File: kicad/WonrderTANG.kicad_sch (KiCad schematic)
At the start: 30 parts, among them CON1 MSX-CONNECTOR, J2 AudioJack3, J3 Conn_02x03_Odd_Even, U1 SN74LVC245AN, U2 SN74LVC245AN, U3 SN74LVC245AN, U48 MCP6281, U5 SN74LVC245AN, U6 Tang_Nano_20k, U7 SN74LVC245AN

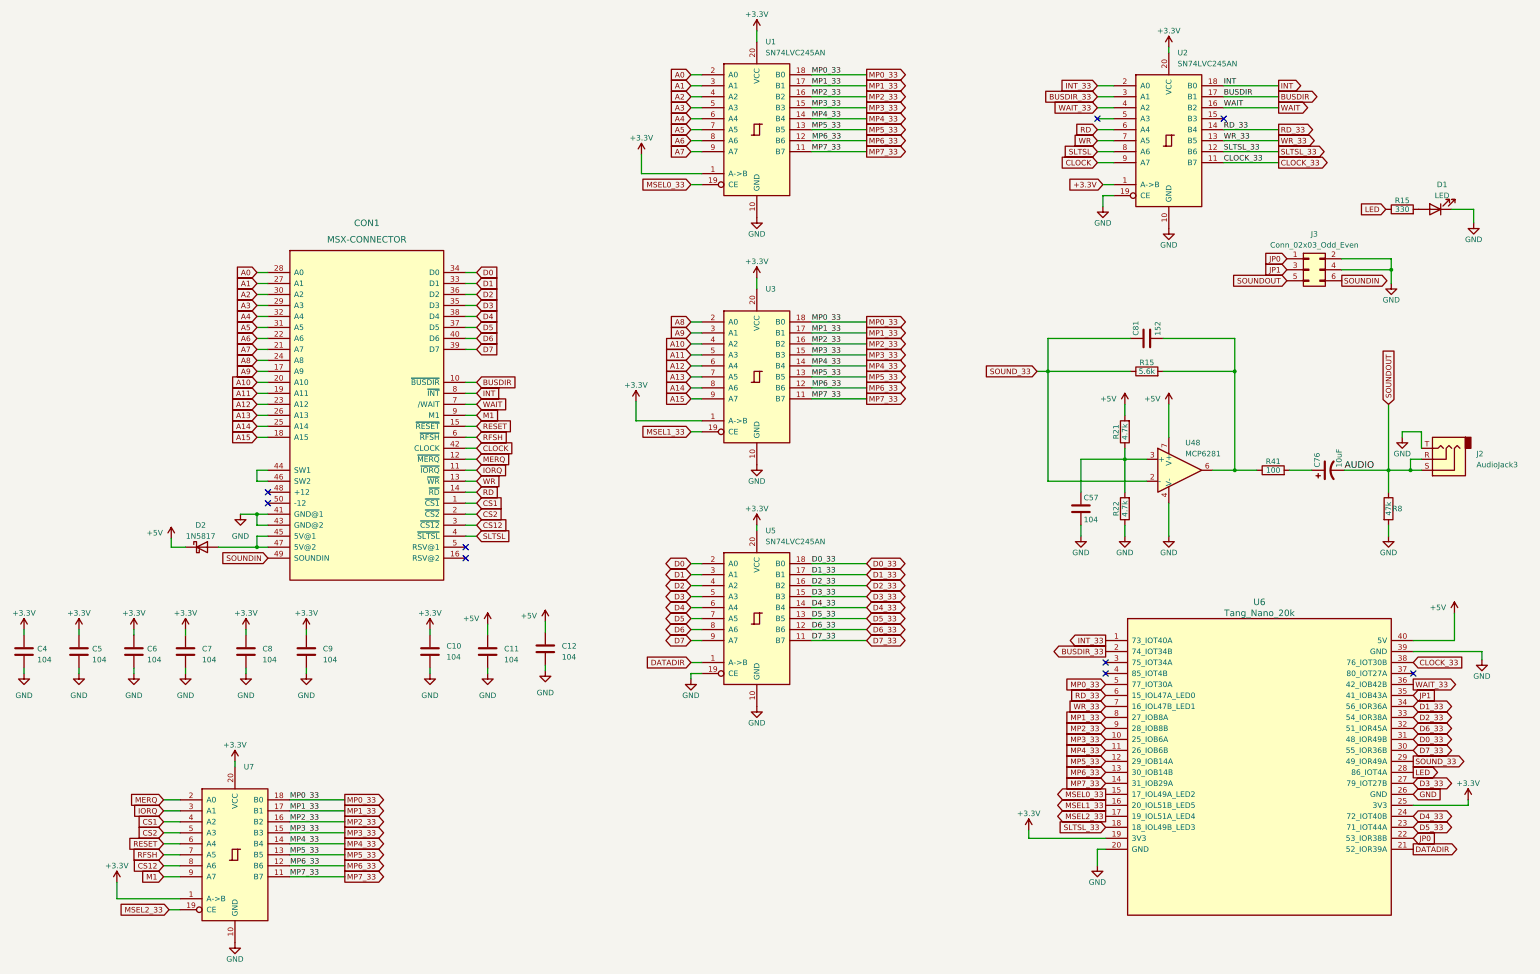
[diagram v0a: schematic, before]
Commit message: fix on wait line
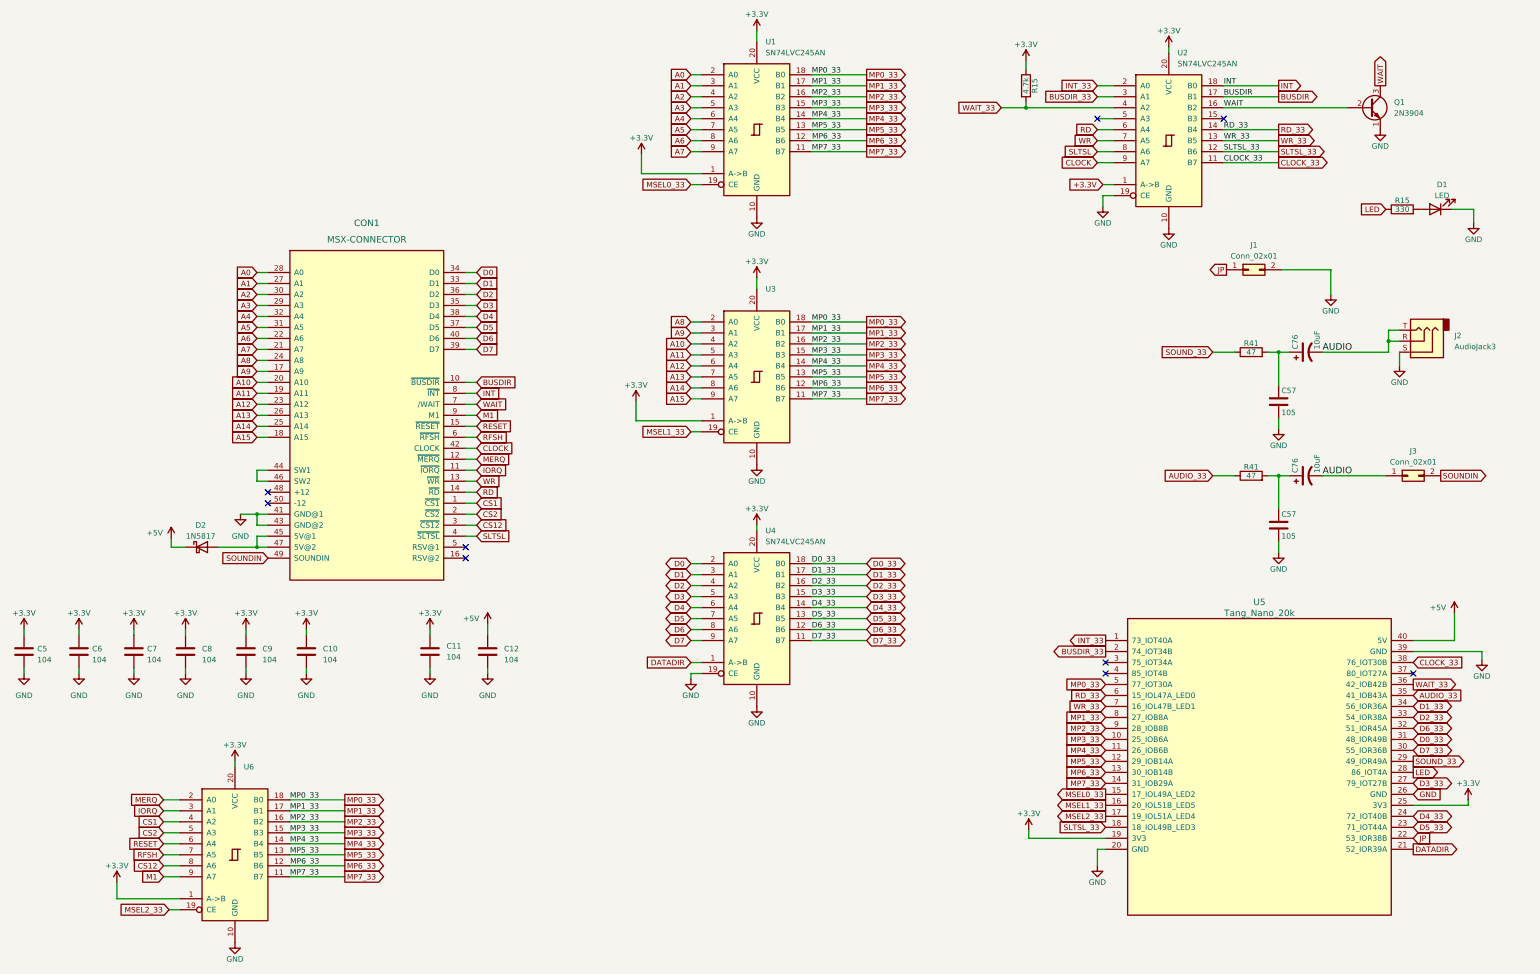
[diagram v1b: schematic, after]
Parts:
- removed C12: 104, Capacitor_THT:C_Disc_D5.0mm_W2.5mm_P2.50mm, symbol Device:C
- removed C81: 152, Capacitor_THT:C_Disc_D5.0mm_W2.5mm_P2.50mm, symbol Device:C
- removed J3: Conn_02x03_Odd_Even, Connector_PinHeader_2.54mm:PinHeader_2x03_P2.54mm_Vertical, symbol Connector_Generic:Conn_02x03_Odd_Even
- removed R21, R22: 4.7k, Resistor_THT:R_Axial_DIN0204_L3.6mm_D1.6mm_P5.08mm_Horizontal, symbol Device:R
- removed R8: 47k, Resistor_THT:R_Axial_DIN0204_L3.6mm_D1.6mm_P5.08mm_Horizontal, symbol Device:R
- removed U48: MCP6281, Package_DIP:DIP-8_W7.62mm_Socket_LongPads, symbol Amplifier_Operational:MCP601-xP
- added C57: 105, Capacitor_THT:C_Disc_D5.0mm_W2.5mm_P2.50mm, symbol Device:C
- added C76: 10uF, Capacitor_THT:CP_Radial_D5.0mm_P2.00mm, symbol Omega-Mainboard-rescue:CP1-Device
- added J1, J3: Conn_02x01, Connector_PinHeader_2.54mm:PinHeader_2x01_P2.54mm_Vertical, symbol Connector_Generic:Conn_02x01
- added Q1: 2N3904, Package_TO_SOT_THT:TO-92_Inline, symbol Transistor_BJT:2N3904
- added R41: 47, Resistor_THT:R_Axial_DIN0207_L6.3mm_D2.5mm_P10.16mm_Horizontal, symbol Device:R
- C57: value 104 -> 105
- R15: footprint Resistor_THT:R_Axial_DIN0204_L3.6mm_D1.6mm_P5.08mm_Horizontal -> Resistor_THT:R_Axial_DIN0207_L6.3mm_D2.5mm_P10.16mm_Horizontal
- R15: value 5.6k -> 4.7k; footprint Resistor_THT:R_Axial_DIN0204_L3.6mm_D1.6mm_P5.08mm_Horizontal -> Resistor_THT:R_Axial_DIN0207_L6.3mm_D2.5mm_P10.16mm_Horizontal
- R41: value 100 -> 47; footprint Resistor_THT:R_Axial_DIN0204_L3.6mm_D1.6mm_P5.08mm_Horizontal -> Resistor_THT:R_Axial_DIN0207_L6.3mm_D2.5mm_P10.16mm_Horizontal
- renumbered C9 to C10, C10 to C11, C11 to C12, C4 to C5, C5 to C6, C6 to C7, C7 to C8, C8 to C9, U5 to U4, U6 to U5, U7 to U6
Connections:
- net +3.3V: now also R15.1
- net GND: now also J2.S, C57.2, J1.2 (Pin_2), Q1.1 (E); no longer J2.T
- net SOUNDIN: now also J3.2 (Pin_2)
- net SOUND_33: now also R41.1; no longer R15.1
- net WAIT: now also Q1.2 (B), Q1.3 (C)
- net WAIT_33: now also R15.2
- net at C57.1: now also C76.1, R41.2
- net JP0 renamed JP
- net JP: now also J1.1 (Pin_1)
- net JP1 renamed AUDIO_33
- net AUDIO_33: now also R41.1
- net SOUNDOUT renamed AUDIO
- net AUDIO: now also J2.T, C76.2, J3.1 (Pin_1); no longer J2.S
- new net: C57.1, C76.1, R41.2
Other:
- moved on the sheet: C57, C76, J2, R41

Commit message: kicad fixes
fix shorted transistor add 10uf power line, moved cap to allow be placed horizontally
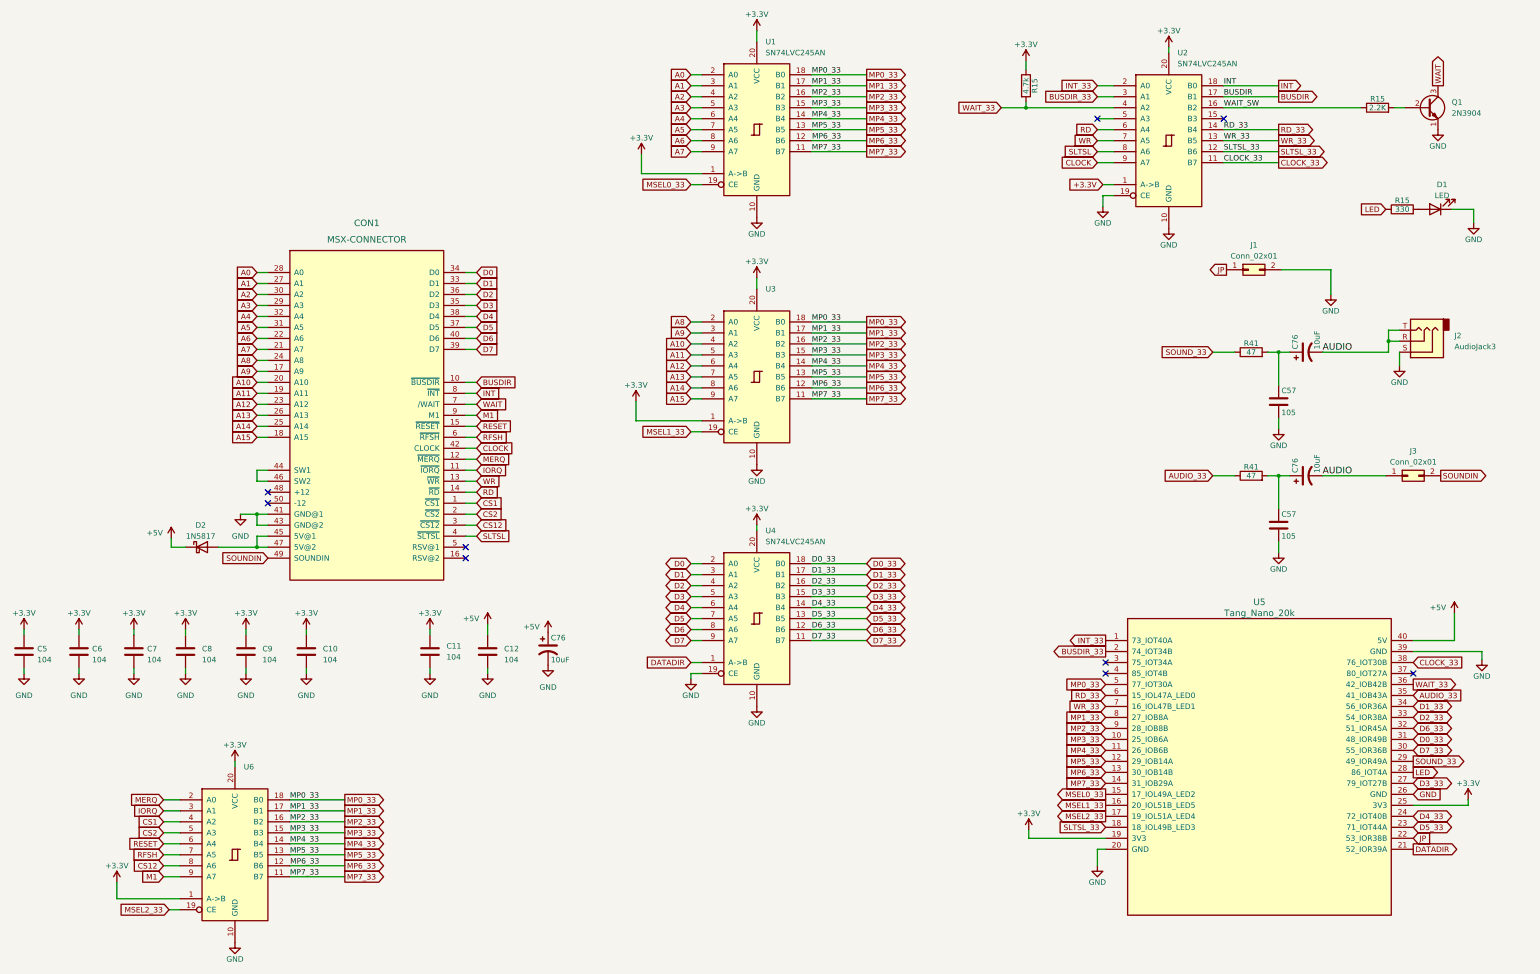
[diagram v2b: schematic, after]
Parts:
- added C76: 10uF, Capacitor_THT:CP_Radial_D5.0mm_P2.00mm, symbol Omega-Mainboard-rescue:CP1-Device
- added R15: 2.2K, Resistor_THT:R_Axial_DIN0207_L6.3mm_D2.5mm_P10.16mm_Horizontal, symbol Device:R
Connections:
- net +5V: now also C76.1
- net GND: now also C76.2
- net WAIT: no longer Q1.2 (B), U2.16 (B2)
- new net: Q1.2 (B), R15.2
- new net WAIT_SW: R15.1, U2.16 (B2)
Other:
- moved on the sheet: Q1
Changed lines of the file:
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@@
     (stroke (width 0) (type default))
   )
-  (wire (pts (xy 325.12 53.34) (xy 353.695 53.34))
-    (stroke (width 0) (type default))
-  )
   (wire (pts (xy 363.22 109.855) (xy 363.22 107.315))
     (stroke (width 0) (type default))
@@
     (stroke (width 0) (type default))
   )
+  (wire (pts (xy 364.49 53.34) (xy 367.03 53.34))
+    (stroke (width 0) (type default))
+  )
   (wire (pts (xy 378.46 176.53) (xy 378.46 170.18))
     (stroke (width 0) (type default))
@@
     (stroke (width 0) (type default))
   )
+  (wire (pts (xy 325.12 53.34) (xy 356.87 53.34))
+    (stroke (width 0) (type default))
+  )
   (wire (pts (xy 97.79 147.32) (xy 101.6 147.32))
     (stroke (width 0) (type default))
@@
     (effects (font (size 1.27 1.27)) (justify left bottom))
   )
-  (label "WAIT" (at 325.12 53.34 0) (fields_autoplaced)
+  (label "WAIT_SW" (at 325.12 53.34 0) (fields_autoplaced)
     (effects (font (size 1.27 1.27)) (justify left bottom))
   )
@@
     )
   )
-  (global_label "WAIT" (shape output) (at 361.315 48.26 90) (fields_autoplaced)
+  (global_label "WAIT" (shape output) (at 374.65 48.26 90) (fields_autoplaced)
     (effects (font (size 1.27 1.27)) (justify left))
-    (property "Intersheetrefs" "${INTERSHEET_REFS}" (at 361.315 41.8166 90)
+    (property "Intersheetrefs" "${INTERSHEET_REFS}" (at 374.65 41.8166 90)
       (effects (font (size 1.27 1.27)) (justify left) hide)
     )
@@
     )
   )
-  (symbol (lib_id "power:GND") (at 361.315 58.42 0) (unit 1)
+  (symbol (lib_id "power:GND") (at 374.65 58.42 0) (unit 1)
     (in_bom yes) (on_board yes) (dnp no)
-    (property "Reference" "#PWR091" (at 361.315 64.77 0)
+    (property "Reference" "#PWR091" (at 374.65 64.77 0)
       (effects (font (size 1.27 1.27)) hide)
     )
-    (property "Value" "GND" (at 361.315 62.23 0)
+    (property "Value" "GND" (at 374.65 62.23 0)
       (effects (font (size 1.27 1.27)))
     )
-    (property "Footprint" "" (at 361.315 58.42 0)
+    (property "Footprint" "" (at 374.65 58.42 0)
       (effects (font (size 1.27 1.27)) hide)
     )
-    (property "Datasheet" "" (at 361.315 58.42 0)
+    (property "Datasheet" "" (at 374.65 58.42 0)
       (effects (font (size 1.27 1.27)) hide)
     )
@@
     )
   )
+  (symbol (lib_id "power:GND") (at 168.91 182.245 0) (unit 1)
+    (in_bom yes) (on_board yes) (dnp no) (fields_autoplaced)
+    (property "Reference" "#PWR047" (at 168.91 188.595 0)
+      (effects (font (size 1.27 1.27)) hide)
+    )
+    (property "Value" "GND" (at 168.91 187.325 0)
+      (effects (font (size 1.27 1.27)))
+    )
+    (property "Footprint" "" (at 168.91 182.245 0)
+      (effects (font (size 1.27 1.27)) hide)
+    )
+    (property "Datasheet" "" (at 168.91 182.245 0)
+      (effects (font (size 1.27 1.27)) hide)
+    )
+    (pin "1")
+    (instances
+      (project "WonrderTANG"
+        (path "/aac9604b-8c84-42de-bd09-e07036aaaac8"
+          (reference "#PWR047") (unit 1)
+        )
+      )
+    )
+  )
   (symbol (lib_id "Device:LED") (at 374.015 76.835 180) (unit 1)
     (in_bom yes) (on_board yes) (dnp no) (fields_autoplaced)
@@
     )
   )
+  (symbol (lib_id "Omega-Mainboard-rescue:CP1-Device") (at 168.91 178.435 0) (unit 1)
+    (in_bom yes) (on_board yes) (dnp no)
+    (property "Reference" "C76" (at 169.545 175.895 0)
+      (effects (font (size 1.27 1.27)) (justify left))
+    )
+    (property "Value" "10uF" (at 169.545 180.975 0)
+      (effects (font (size 1.27 1.27)) (justify left))
+    )
+    (property "Footprint" "Capacitor_THT:CP_Radial_D5.0mm_P2.00mm" (at 168.91 178.435 0)
+      (effects (font (size 1.27 1.27)) hide)
+    )
+    (property "Datasheet" "" (at 168.91 178.435 0)
+      (effects (font (size 1.27 1.27)) hide)
+    )
+    (pin "1")
+    (pin "2")
+    (instances
+      (project "Omega-Mainboard"
+        (path "/494667ff-8681-4396-86d5-0cbe152842af/00000000-0000-0000-0000-00005bf99f40"
+          (reference "C76") (unit 1)
+        )
+      )
+      (project "WonrderTANG"
+        (path "/aac9604b-8c84-42de-bd09-e07036aaaac8"
+          (reference "C13") (unit 1)
+        )
+      )
+    )
+  )
   (symbol (lib_id "Connector_Audio:AudioJack3") (at 370.84 107.315 180) (unit 1)
     (in_bom yes) (on_board yes) (dnp no) (fields_autoplaced)
@@
     )
   )
+  (symbol (lib_id "Device:R") (at 360.68 53.34 90) (unit 1)
+    (in_bom yes) (on_board yes) (dnp no)
+    (property "Reference" "R15" (at 360.68 51.308 90)
+      (effects (font (size 1.27 1.27)))
+    )
+    (property "Value" "2.2K" (at 360.68 53.34 90)
+      (effects (font (size 1.27 1.27)))
+    )
+    (property "Footprint" "Resistor_THT:R_Axial_DIN0207_L6.3mm_D2.5mm_P10.16mm_Horizontal" (at 360.68 55.118 90)
+      (effects (font (size 1.27 1.27)) hide)
+    )
+    (property "Datasheet" "" (at 360.68 53.34 0)
+      (effects (font (size 1.27 1.27)) hide)
+    )
+    (pin "1")
+    (pin "2")
+    (instances
+      (project "Omega-Mainboard"
+        (path "/494667ff-8681-4396-86d5-0cbe152842af/00000000-0000-0000-0000-00005bf99f40"
+          (reference "R15") (unit 1)
+        )
+      )
+      (project "WonrderTANG"
+        (path "/aac9604b-8c84-42de-bd09-e07036aaaac8"
+          (reference "R5") (unit 1)
+        )
+      )
+    )
+  )
   (symbol (lib_id "power:GND") (at 99.06 184.15 0) (unit 1)
     (in_bom yes) (on_board yes) (dnp no) (fields_autoplaced)
@@
     )
   )
-  (symbol (lib_id "Transistor_BJT:2N3904") (at 358.775 53.34 0) (unit 1)
+  (symbol (lib_id "Transistor_BJT:2N3904") (at 372.11 53.34 0) (unit 1)
     (in_bom yes) (on_board yes) (dnp no) (fields_autoplaced)
-    (property "Reference" "Q1" (at 364.49 52.07 0)
+    (property "Reference" "Q1" (at 377.825 52.07 0)
       (effects (font (size 1.27 1.27)) (justify left))
     )
-    (property "Value" "2N3904" (at 364.49 54.61 0)
+    (property "Value" "2N3904" (at 377.825 54.61 0)
       (effects (font (size 1.27 1.27)) (justify left))
     )
-    (property "Footprint" "Package_TO_SOT_THT:TO-92_Inline" (at 363.855 55.245 0)
+    (property "Footprint" "Package_TO_SOT_THT:TO-92_Inline" (at 377.19 55.245 0)
       (effects (font (size 1.27 1.27) italic) (justify left) hide)
     )
-    (property "Datasheet" "https://www.onsemi.com/pub/Collateral/2N3903-D.PDF" (at 358.775 53.34 0)
+    (property "Datasheet" "https://www.onsemi.com/pub/Collateral/2N3903-D.PDF" (at 372.11 53.34 0)
       (effects (font (size 1.27 1.27)) (justify left) hide)
     )
@@
         )
       )
+    )
+  )
+  (symbol (lib_id "power:+5V") (at 168.91 174.625 0) (unit 1)
+    (in_bom yes) (on_board yes) (dnp no)
+    (property "Reference" "#PWR046" (at 168.91 178.435 0)
+      (effects (font (size 1.27 1.27)) hide)
+    )
+    (property "Value" "+5V" (at 165.1 173.355 0)
+      (effects (font (size 1.27 1.27)))
+    )
+    (property "Footprint" "" (at 168.91 174.625 0)
+      (effects (font (size 1.27 1.27)) hide)
+    )
+    (property "Datasheet" "" (at 168.91 174.625 0)
+      (effects (font (size 1.27 1.27)) hide)
+    )
+    (pin "1")
+    (instances
+      (project "WonrderTANG"
+        (path "/aac9604b-8c84-42de-bd09-e07036aaaac8"
+          (reference "#PWR046") (unit 1)
+        )
+      )

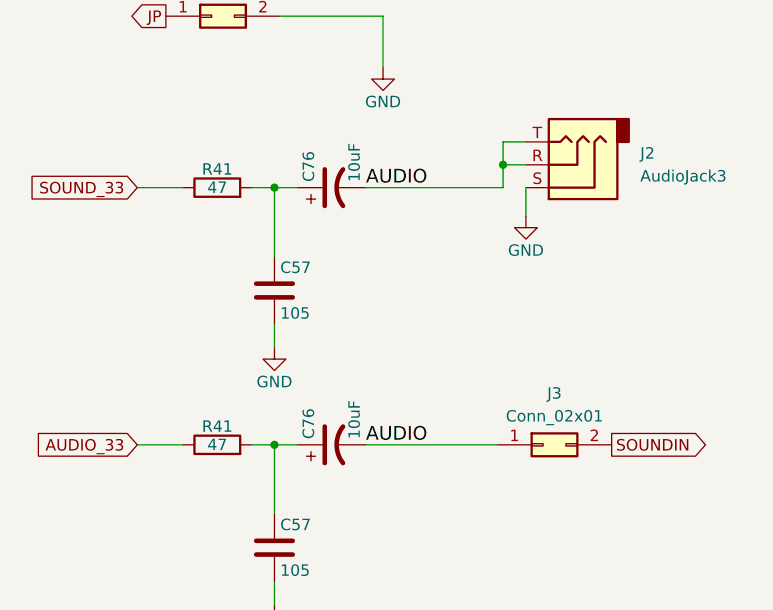
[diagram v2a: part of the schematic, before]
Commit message: Fix board audio
audio pins were connected together
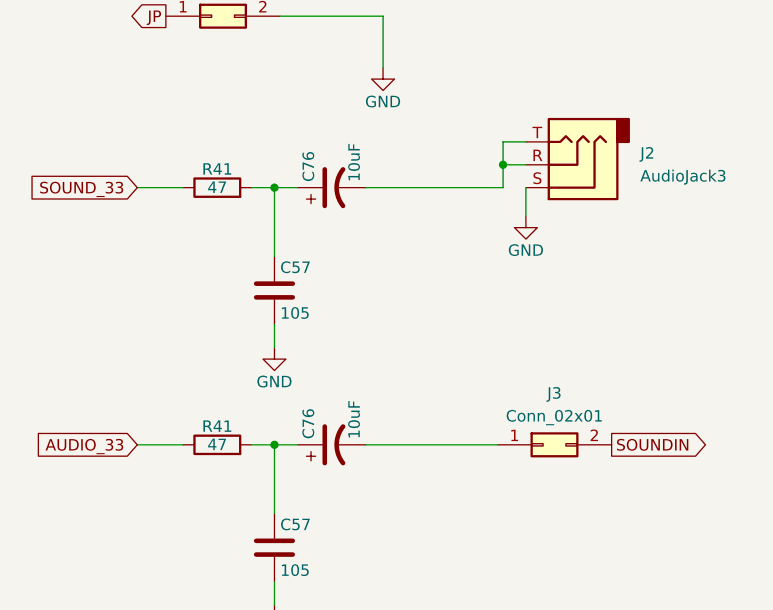
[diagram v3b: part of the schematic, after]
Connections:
- net AUDIO: no longer names the net of C76.2, J2.R, J2.T
- net AUDIO: no longer C76.2, J3.1 (Pin_1)
- new net: C76.2, J3.1 (Pin_1)
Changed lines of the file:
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@@
     (effects (font (size 1.27 1.27)) (justify left bottom))
-  )
-  (label "AUDIO" (at 347.98 138.43 0) (fields_autoplaced)
-    (effects (font (size 1.524 1.524)) (justify left bottom))
   )
   (label "MP7_33" (at 229.87 63.5 0) (fields_autoplaced)
@@
     (effects (font (size 1.27 1.27)) (justify left bottom))
   )
-  (label "AUDIO" (at 347.98 109.855 0) (fields_autoplaced)
-    (effects (font (size 1.524 1.524)) (justify left bottom))
-  )
   (label "MP6_33" (at 109.2711 228.6 0) (fields_autoplaced)
